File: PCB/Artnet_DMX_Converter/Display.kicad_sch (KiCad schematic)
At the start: 1 part, among them J12 IDC

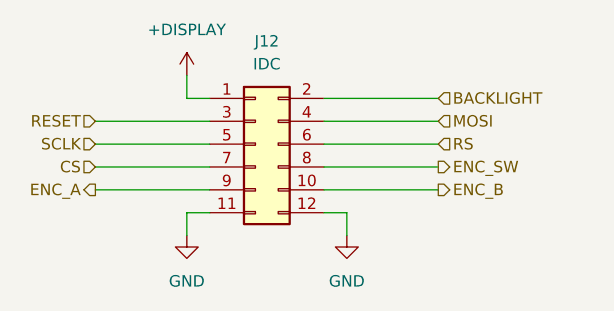
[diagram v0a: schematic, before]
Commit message: Updated the PCB Allot
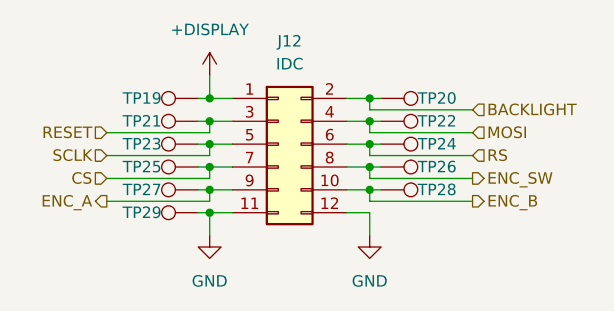
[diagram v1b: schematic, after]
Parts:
- added TP19, TP20, TP21, TP22, TP23, TP24, TP25, TP26, TP27, TP28, TP29: TestPoint, TestPoint:TestPoint_Pad_D1.5mm, symbol Connector:TestPoint
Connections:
- net +DISPLAY: now also TP19.1
- net BACKLIGHT: now also TP20.1
- net CS: now also TP25.1
- net ENC_A: now also TP27.1
- net ENC_B: now also TP28.1
- net ENC_SW: now also TP26.1
- net GND: now also TP29.1
- net MOSI: now also TP22.1
- net RESET: now also TP21.1
- net RS: now also TP24.1
- net SCLK: now also TP23.1
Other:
- moved on the sheet: J12
